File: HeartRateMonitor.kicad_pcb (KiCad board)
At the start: 2 copper layers, 30 x 46.5 mm, 31 parts, among them J1 USB_C_Receptacle_USB2.0, J2 SWD, J3 Conn_01x08_Pin, U1 CH340E, U3 TLV62130, U4 STM32G030F6Px

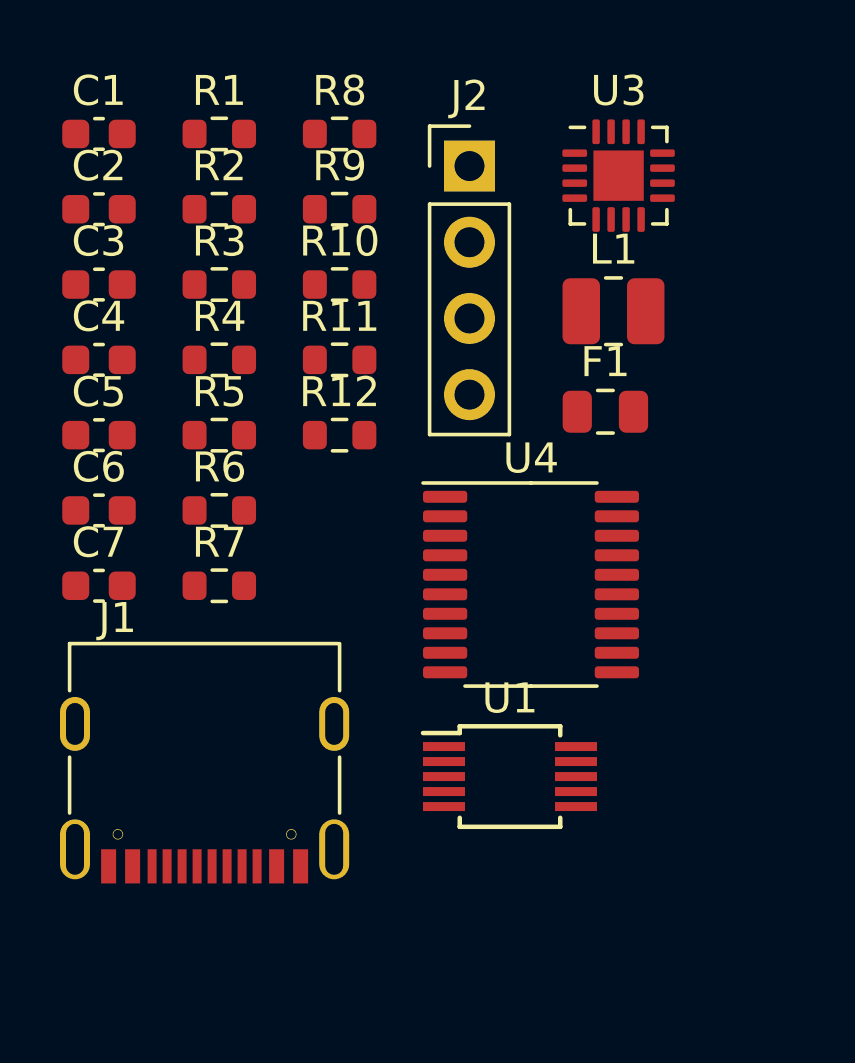
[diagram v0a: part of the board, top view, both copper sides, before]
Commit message: low and high pass filter
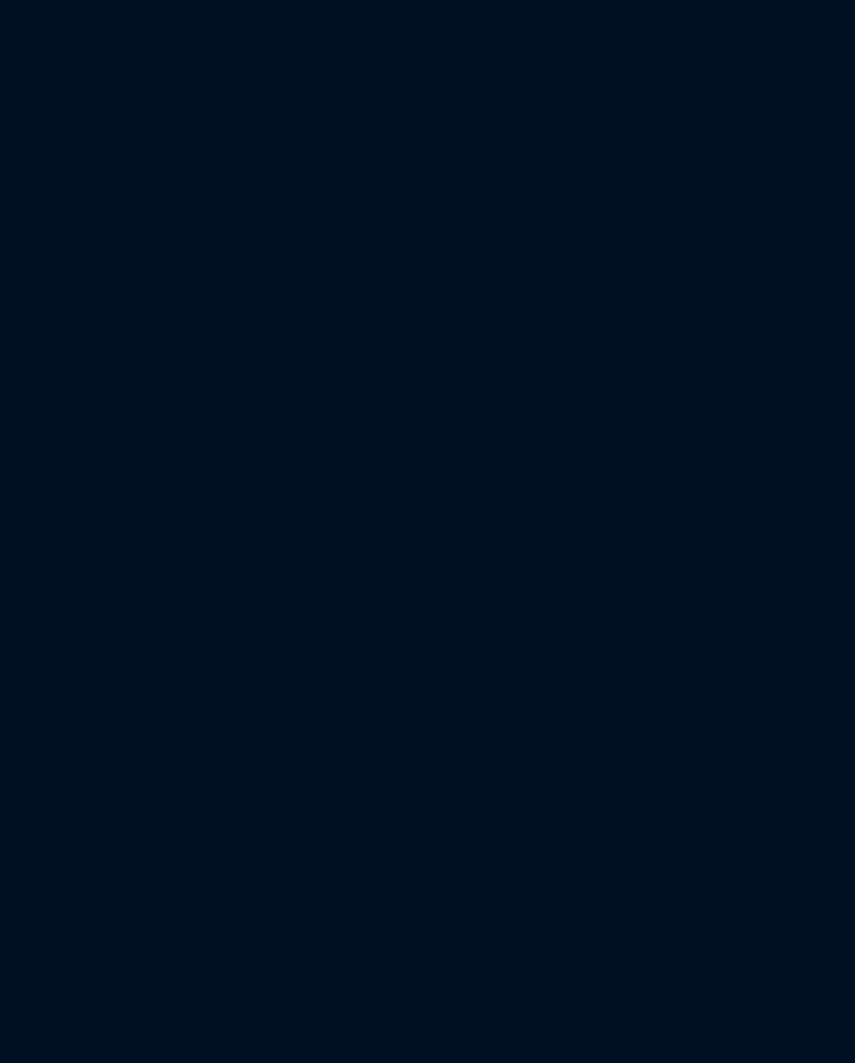
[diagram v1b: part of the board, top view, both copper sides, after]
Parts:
- removed C1, C2, C3, C5: 100nF, Capacitor_SMD:C_0603_1608Metric
- removed C4: 10uF, Capacitor_SMD:C_0603_1608Metric
- removed C6: 470pF, Capacitor_SMD:C_0603_1608Metric
- removed C7: 22uF, Capacitor_SMD:C_0603_1608Metric
- removed F1: 2A, Fuse:Fuse_0805_2012Metric
- removed J1: USB_C_Receptacle_USB2.0, FP:TYPE-C-31-M-31
- removed J2: SWD, Connector_PinHeader_2.54mm:PinHeader_1x04_P2.54mm_Vertical
- removed L1: HEI252012A-2R2M-Q8, Inductor_SMD:L_1008_2520Metric
- removed R1, R2: 5K1, Resistor_SMD:R_0603_1608Metric
- removed R10, R11, R12, R6, R7, R9: 0, Resistor_SMD:R_0603_1608Metric
- removed R3: 1M, Resistor_SMD:R_0603_1608Metric
- removed R4: 562K, Resistor_SMD:R_0603_1608Metric
- removed R5: 180K, Resistor_SMD:R_0603_1608Metric
- removed R8: 100K, Resistor_SMD:R_0603_1608Metric
- removed U1: CH340E, Package_SO:MSOP-10_3x3mm_P0.5mm
- removed U3: TLV62130, Package_DFN_QFN:VQFN-16-1EP_3x3mm_P0.5mm_EP1.68x1.68mm
- removed U4: STM32G030F6Px, Package_SO:TSSOP-20_4.4x6.5mm_P0.65mm

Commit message: refactor
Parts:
- added C1: 100nF, Capacitor_SMD:C_0603_1608Metric, F.Cu at (136.5, 95.5)
- added C10: 1uF, Capacitor_SMD:C_0603_1608Metric, F.Cu at (140.6, 95.5)
- added C11: 1uF, Capacitor_SMD:C_0603_1608Metric, F.Cu at (140.6, 98.1)
- added C12: 20.5uF, Capacitor_SMD:C_0603_1608Metric, F.Cu at (140.6, 100.6)
- added C13: 17.8uF, Capacitor_SMD:C_0603_1608Metric, F.Cu at (140.6, 103.1)
- added C14: 100nF, Capacitor_SMD:C_0603_1608Metric, F.Cu at (140.6, 105.6)
- added C15: 205nF, Capacitor_SMD:C_0603_1608Metric, F.Cu at (140.6, 108.1)
- added C16: 10uF, Capacitor_SMD:C_0603_1608Metric, F.Cu at (140.6, 110.6)
- added C17: 20.5uF, Capacitor_SMD:C_0603_1608Metric, F.Cu at (140.6, 113.1)
- added C18: 10uF, Capacitor_SMD:C_0603_1608Metric, F.Cu at (140.6, 115.6)
- added C19: 100nF, Capacitor_SMD:C_0603_1608Metric, F.Cu at (144.6, 95.5)
- added C2: 100nF, Capacitor_SMD:C_0603_1608Metric, F.Cu at (136.5, 98.1)
- added C20: 1uF, Capacitor_SMD:C_0603_1608Metric, F.Cu at (144.6, 98.1)
- added C3: 100nF, Capacitor_SMD:C_0603_1608Metric, F.Cu at (136.5, 100.6)
- added C4: 10uF, Capacitor_SMD:C_0603_1608Metric, F.Cu at (136.5, 103.1)
- added C5: 100nF, Capacitor_SMD:C_0603_1608Metric, F.Cu at (136.5, 105.6)
- added C6: 470pF, Capacitor_SMD:C_0603_1608Metric, F.Cu at (136.5, 108.1)
- added C7: 22uF, Capacitor_SMD:C_0603_1608Metric, F.Cu at (136.5, 110.6)
- added C8: 150pF, Capacitor_SMD:C_0603_1608Metric, F.Cu at (136.5, 113.1)
- added C9: 1uF, Capacitor_SMD:C_0603_1608Metric, F.Cu at (136.5, 115.6)
- added D1: VEMD5510C, FP:VEMD5510C, F.Cu at (160.5, 107.3)
- added F1: 2A, Fuse:Fuse_0805_2012Metric, F.Cu at (156.8, 126.2)
- added J1: USB_C_Receptacle_USB2.0, FP:TYPE-C-31-M-31, F.Cu at (140.1, 122.6)
- added J2: SWD, Connector_PinHeader_2.54mm:PinHeader_1x04_P2.54mm_Vertical, F.Cu at (162.1, 96.6)
- added L1: HEI252012A-2R2M-Q8, Inductor_SMD:L_1008_2520Metric, F.Cu at (157.1, 122.9)
- added R1: 5K1, Resistor_SMD:R_0603_1608Metric, F.Cu at (144.6, 100.6)
- added R10: 0, Resistor_SMD:R_0603_1608Metric, F.Cu at (148.6, 100.6)
- added R11: 0, Resistor_SMD:R_0603_1608Metric, F.Cu at (148.6, 103.1)
- added R12: 0, Resistor_SMD:R_0603_1608Metric, F.Cu at (148.6, 105.6)
- added R13: 500K, Resistor_SMD:R_0603_1608Metric, F.Cu at (148.6, 108.1)
- added R14: 4K22, Resistor_SMD:R_0603_1608Metric, F.Cu at (148.6, 110.6)
- added R15: 1K15, Resistor_SMD:R_0603_1608Metric, F.Cu at (148.6, 113.1)
- added R16: 2K37, Resistor_SMD:R_0603_1608Metric, F.Cu at (148.6, 115.6)
- added R17: 3K24, Resistor_SMD:R_0603_1608Metric, F.Cu at (152.6, 95.5)
- added R18: 2K37, Resistor_SMD:R_0603_1608Metric, F.Cu at (152.6, 98.1)
- added R19: 3K24, Resistor_SMD:R_0603_1608Metric, F.Cu at (152.6, 100.6)
- added R2: 5K1, Resistor_SMD:R_0603_1608Metric, F.Cu at (144.6, 103.1)
- added R20: 10K, Resistor_SMD:R_0603_1608Metric, F.Cu at (152.6, 103.1)
- added R21: 10K, Resistor_SMD:R_0603_1608Metric, F.Cu at (152.6, 105.6)
- added R22: 1K, Resistor_SMD:R_0603_1608Metric, F.Cu at (152.6, 108.1)
- added R3: 1M, Resistor_SMD:R_0603_1608Metric, F.Cu at (144.6, 105.6)
- added R4: 562K, Resistor_SMD:R_0603_1608Metric, F.Cu at (144.6, 108.1)
- added R5: 180K, Resistor_SMD:R_0603_1608Metric, F.Cu at (144.6, 110.6)
- added R6: 0, Resistor_SMD:R_0603_1608Metric, F.Cu at (144.6, 113.1)
- added R7: 0, Resistor_SMD:R_0603_1608Metric, F.Cu at (144.6, 115.6)
- added R8: 100K, Resistor_SMD:R_0603_1608Metric, F.Cu at (148.6, 95.5)
- added R9: 0, Resistor_SMD:R_0603_1608Metric, F.Cu at (148.6, 98.1)
- added U1: CH340E, Package_SO:MSOP-10_3x3mm_P0.5mm, F.Cu at (163.4, 115.8)
- added U10: TLV9301, Package_TO_SOT_SMD:SOT-23-5, F.Cu at (157.2, 118.8)
- added U2: TLV9301, Package_TO_SOT_SMD:SOT-23-5, F.Cu at (157.2, 96.5)
- added U3: TLV62130, Package_DFN_QFN:VQFN-16-1EP_3x3mm_P0.5mm_EP1.68x1.68mm, F.Cu at (162.4, 120.8)
- added U4: STM32G030F6Px, Package_SO:TSSOP-20_4.4x6.5mm_P0.65mm, F.Cu at (150.0, 120.9)
- added U5: TPS60403, Package_TO_SOT_SMD:SOT-23-5, F.Cu at (157.2, 101.0)
- added U6: TLV9301, Package_TO_SOT_SMD:SOT-23-5, F.Cu at (157.2, 105.4)
- added U7: TLV9301, Package_TO_SOT_SMD:SOT-23-5, F.Cu at (157.2, 109.9)
- added U8: TLV9301, Package_TO_SOT_SMD:SOT-23-5, F.Cu at (157.2, 114.3)
- added U9: AD5272BCP, Package_CSP:LFCSP-WD-10-1EP_3x3mm_P0.5mm_EP1.64x2.38mm, F.Cu at (162.4, 125.7)

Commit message: layout
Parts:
- C18, C19, C20, C7, C8, D1, J2, R1, R13, R2, R20, R21, R22, R5, U10, U2, U9: moved to B.Cu
- moved U2 64.4 mm to (107.2, 137.2), turned to -90 degrees
- moved D1 62.7 mm to (106.8, 139.8), turned to -90 degrees
- moved U6 53.2 mm to (110.2, 130.3), turned to 90 degrees
- moved U1 52.4 mm to (111.0, 116.9)
- moved U5 51.7 mm to (122.1, 138.9)
- moved U3 51.2 mm to (112.6, 108.8), turned to 180 degrees
- moved R17 50.0 mm to (115.2, 128.7)
- moved C10 49.6 mm to (119.1, 140.2), turned to -90 degrees
- moved F1 49.5 mm to (109.0, 113.7)
- moved R13 47.4 mm to (111.7, 137.8), turned to 90 degrees
- moved U9 47.3 mm to (115.5, 132.2), turned to 90 degrees
- moved C20 46.2 mm to (112.9, 131.6), turned to 90 degrees
- moved C19 45.4 mm to (113.4, 128.5), turned to -90 degrees
- moved U10 44.9 mm to (115.8, 136.2)
- moved R15 44.5 mm to (109.2, 133.9), turned to 90 degrees
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
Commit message: modify latout
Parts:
- C12, C13, R14, R15, R8, U6: moved to B.Cu
- C18, C19, C20, R20, R21, R22, U10, U9: moved to F.Cu
- moved C6 35.5 mm to (107.2, 142.9), turned to -90 degrees
- moved C5 33.8 mm to (108.8, 142.8), turned to -90 degrees
- moved C4 32.3 mm to (110.4, 142.8), turned to -90 degrees
- moved R5 31.6 mm to (107.2, 138.5), turned to 90 degrees
- moved U3 30.6 mm to (108.6, 139.2), turned to -90 degrees
- moved R4 29.4 mm to (107.2, 135.4), turned to 90 degrees
- moved J1 29.2 mm to (118.6, 141.9), turned to 180 degrees
- moved L1 26.4 mm to (109.4, 134.9), turned to 90 degrees
- moved J2 25.7 mm to (102.5, 115.7)
- moved C1 25.6 mm to (126.3, 139.2), turned to 90 degrees
- moved R3 25.4 mm to (124.7, 139.2), turned to -90 degrees
- moved C7 24.1 mm to (111.6, 135.4), turned to -90 degrees
- moved F1 24.0 mm to (115.6, 136.8), turned to 90 degrees
- moved R2 22.6 mm to (117.5, 136.5), turned to 90 degrees
- moved C16 22.1 mm to (127.7, 108.6), turned to 90 degrees
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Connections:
- U4 pad 16: unconnected-(U4-PA11/PA9-Pad16) -> /DIGIPOT_SCL
- U4 pad 17: unconnected-(U4-PA12/PA10-Pad17) -> /DIGIPOT_SDA

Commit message: add LED
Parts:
- added D2: VLMTG41S2U1, Capacitor_Tantalum_SMD:CP_EIA-3528-21_Kemet-B, F.Cu at (135.3, 130.7)
- added D3: VLMTG41S2U1, Capacitor_Tantalum_SMD:CP_EIA-3528-21_Kemet-B, F.Cu at (135.3, 135.1)
- added R23: 4.7R, Resistor_SMD:R_0603_1608Metric, F.Cu at (140.3, 129.8)
- added R24: 4.7R, Resistor_SMD:R_0603_1608Metric, F.Cu at (140.3, 132.3)
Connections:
- U4 pad 2: unconnected-(U4-PC14/PB9-Pad2) -> Net-(D2-K)
- U4 pad 3: unconnected-(U4-PC15-Pad3) -> Net-(D3-K)

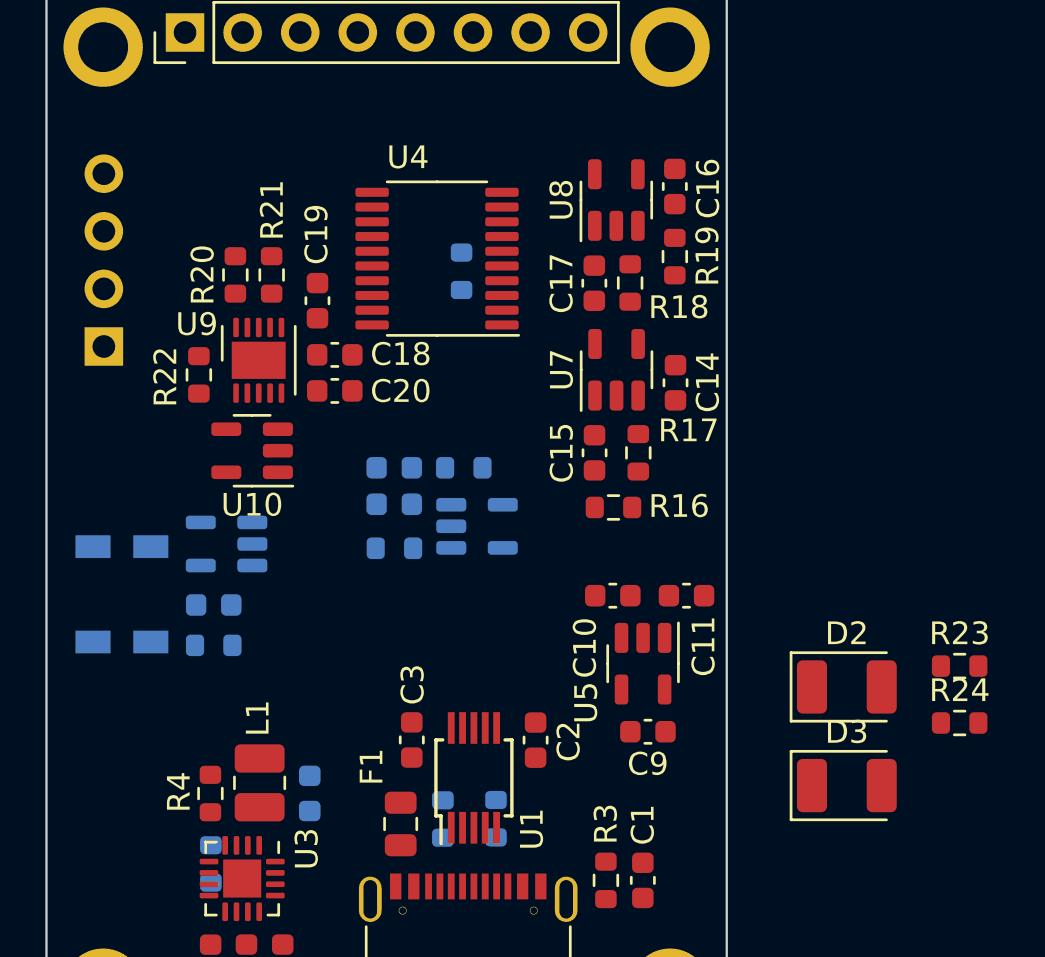
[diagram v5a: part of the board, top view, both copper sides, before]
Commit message: slight modify layout
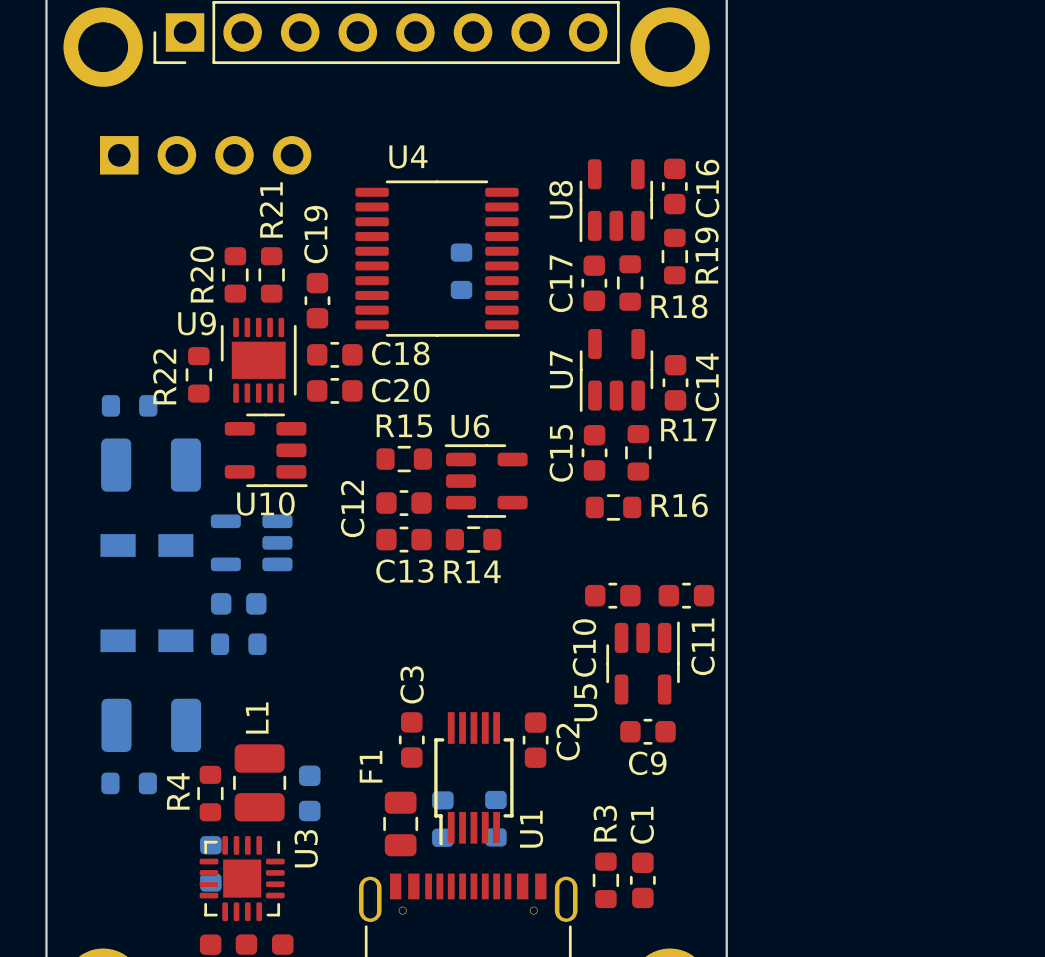
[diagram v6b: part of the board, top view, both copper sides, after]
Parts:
- C12, C13, R14, R15, U6: moved to F.Cu
- D2, D3, R23, R24: moved to B.Cu
- moved R23 38.4 mm to (103.7, 118.3), turned to 180 degrees
- moved R24 36.7 mm to (103.6, 135.0), turned to 180 degrees
- moved D2 32.2 mm to (104.6, 120.9), turned to 180 degrees
- moved D3 30.8 mm to (104.6, 132.4), turned to 180 degrees
- moved J2 8.46 mm to (103.2, 107.3), turned to -90 degrees
- moved R15 3.96 mm to (115.8, 120.7)
- moved C13 3.20 mm to (115.8, 124.2)
- moved R14 3.20 mm to (118.8, 124.2)
- moved U6 2.04 mm to (119.4, 121.6)
- moved C8 1.11 mm to (108.5, 127.0)
- moved D1 1.11 mm to (106.5, 124.0)
- moved U2 1.11 mm to (109.0, 124.4)
- moved R13 1.11 mm to (108.5, 128.8)
- moved U10 0.60 mm to (109.7, 120.3)
- moved C12 0.43 mm to (115.8, 122.6)

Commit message: @...@
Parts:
- C7, R5: moved to F.Cu
- moved R5 2.33 mm to (104.9, 138.4), turned to 0 degrees
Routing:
- net GND: track 0.00 -> 219.1 mm, vias 0 -> 13
- net +3V3: track 0.00 -> 172.7 mm, vias 0 -> 4
- net -3V3: track 0.00 -> 61.1 mm, vias 0 -> 4
- net Net-(D3-K): track 0.00 -> 28.9 mm, vias 0 -> 1
- net /MCU_TX: track 0.00 -> 19.8 mm, vias 0 -> 2
- net /MCU_RX: track 0.00 -> 18.3 mm, vias 0 -> 2
- net +5V: track 0.00 -> 17.3 mm
- net Net-(D2-K): track 0.00 -> 16.8 mm, vias 0 -> 1
- net Net-(J2-Pin_2): track 0.00 -> 16.7 mm, vias 0 -> 2
- net /HIGH_PH: track 0.00 -> 15.4 mm
- net /SCR_BLK: track 0.00 -> 13.5 mm, vias 0 -> 2
- net /AMP_PH: track 0.00 -> 12.9 mm
- net Net-(J2-Pin_3): track 0.00 -> 12.5 mm, vias 0 -> 1
- net /RAW_PH: track 0.00 -> 11.1 mm, vias 0 -> 1
- net /SCR_DATA: track 0.00 -> 10.7 mm
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- added copper zone on F.Cu, net +5V

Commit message: success 1/2 (?)
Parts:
- R1, R2, R8: moved to F.Cu
- moved R11 54.2 mm to (172.2, 73.2)
- moved R10 54.2 mm to (169.3, 76.3)
- moved R12 54.2 mm to (174.7, 73.2)
- moved R7 54.2 mm to (164.9, 73.5)
- moved R9 54.2 mm to (166.8, 76.3)
- moved R6 54.2 mm to (162.4, 73.5)
- moved J2 36.2 mm to (136.4, 92.9)
- moved C5 23.5 mm to (124.8, 125.6), turned to 0 degrees
- moved C15 21.9 mm to (102.5, 117.8)
- moved U7 21.9 mm to (103.4, 114.1)
- moved R17 21.9 mm to (104.4, 117.8)
- moved C14 21.1 mm to (106.8, 115.4), turned to 0 degrees
- moved R23 20.9 mm to (105.4, 139.2)
- moved C10 20.6 mm to (111.9, 142.5)
- moved C4 20.3 mm to (122.3, 126.4), turned to 90 degrees
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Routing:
- net GND: track 219.1 -> 24.1 mm, vias 13 -> 15
- net +3V3: track 172.7 -> 32.0 mm
- net -3V3: track 61.1 -> 0.00 mm, vias 4 -> 0
- net Net-(J2-Pin_2): track 16.7 -> 0.00 mm, vias 2 -> 0
- net /HIGH_PH: track 15.4 -> 0.00 mm
- net Net-(D3-K): track 28.9 -> 13.5 mm, vias 1 -> 0
- net /SCR_BLK: track 13.5 -> 0.00 mm, vias 2 -> 0
- net /AMP_PH: track 12.9 -> 0.00 mm
- net Net-(J2-Pin_3): track 12.5 -> 0.00 mm, vias 1 -> 0
- net /SCR_DATA: track 10.7 -> 0.00 mm
- net +5V: track 17.3 -> 7.39 mm
- net /SCR_SCK: track 9.44 -> 0.00 mm
- net /LOW_PH: track 8.99 -> 0.00 mm
- net /DIGIPOT_SCL: track 8.64 -> 0.00 mm
- net Net-(U6--): track 8.47 -> 0.00 mm
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- added copper zone on B.Cu, net GND
- added copper zone on B.Cu, net Net-(F1-Pad1)
- added copper zone on F.Cu, net Net-(L1-Pad1)
